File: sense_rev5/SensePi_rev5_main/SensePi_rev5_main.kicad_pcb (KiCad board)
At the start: 2 copper layers, 56.5 x 40 mm, 65 parts, among them J1 PJ-611-5A_AudioJack, J2 Conn_02x03_Odd_Even, Q1 IRLML6401, Q2 SI2302, SW1 SW_SPST, SW2 Slider_Switch_SW_2_State, U1 MDBT42Q, U2 MCP4012T-503E/CH, U3 TLV522, U4 PIR, U5 PCF8563T, Y1 Q13FC1350000400, Y2 Q13FC1350000400

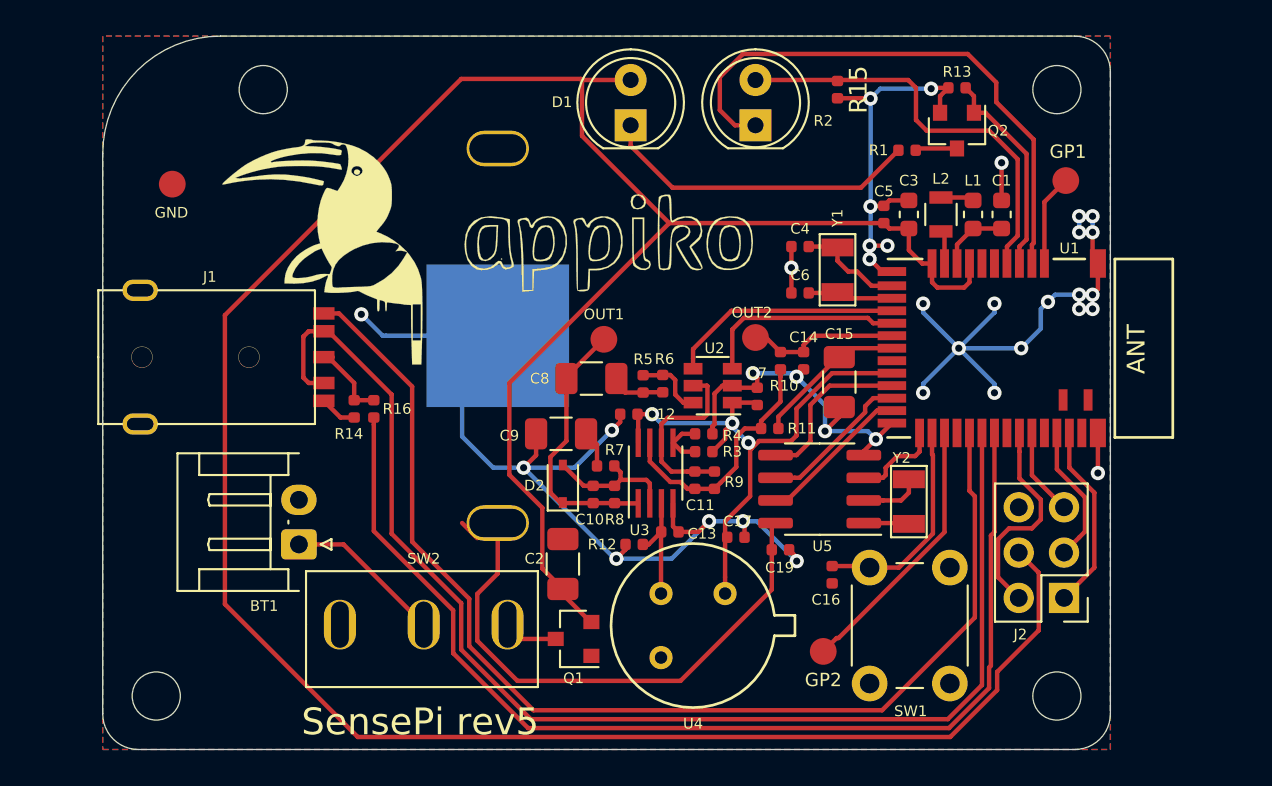
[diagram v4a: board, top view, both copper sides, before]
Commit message: Fix power switch GND conn and other minor fixes
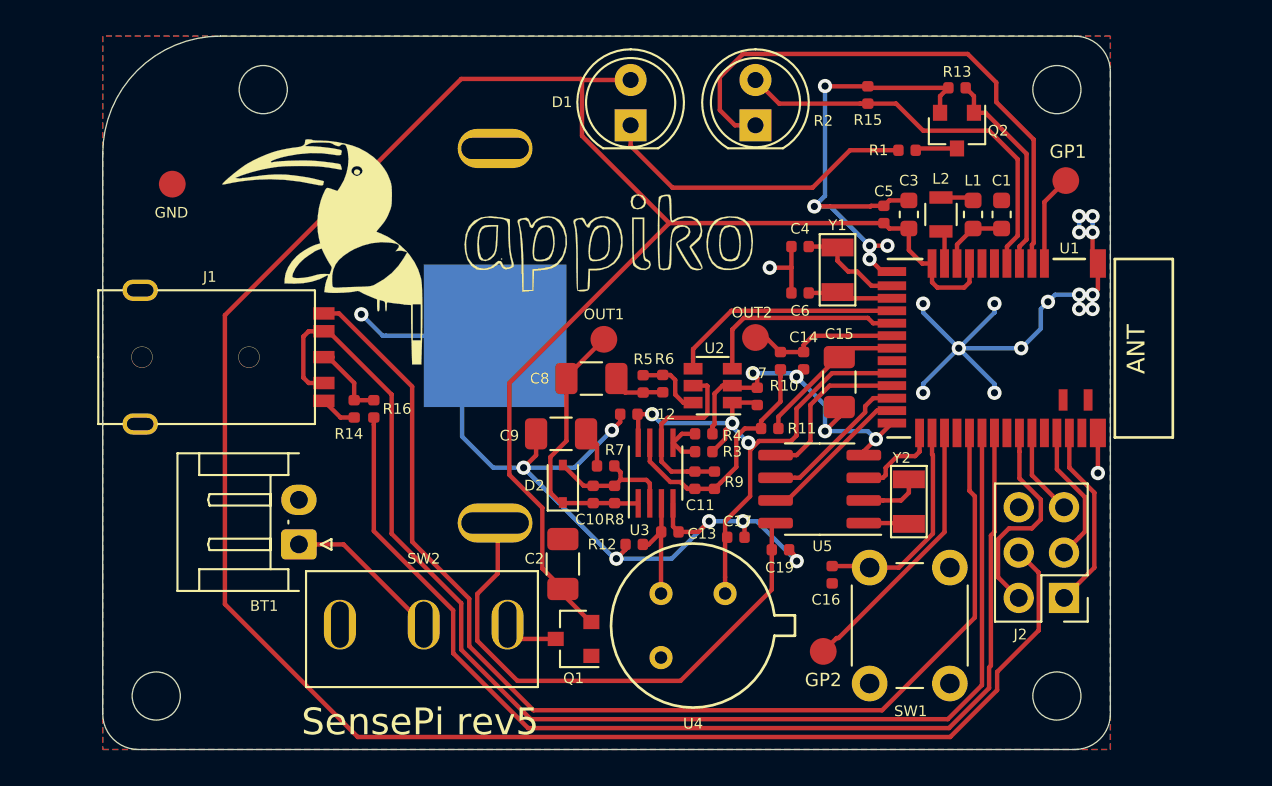
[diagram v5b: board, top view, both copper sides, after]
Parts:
- R14: value 1.2k -> NC
- R16: value 1k -> 470E
- moved G*** 5.02 mm to (56.1, 18.7)
- moved R15 1.73 mm to (52.9, 13.3), turned to 90 degrees
- moved BT2 0.15 mm to (32.0, 26.8)
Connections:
- SW2 pad 1: GND -> Net-(SW2-Pad1)
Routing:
- net GND: track 135.0 -> 140.7 mm, vias 35 -> 33
- net Net-(BT2-Pad1): track 31.7 -> 30.5 mm
- net /LDR_SENSE: track 23.7 -> 22.6 mm

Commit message: senseBe_rev4 and sense_rev5 gerber files updated.
senseBe_rev4 and sense_rev5 Slider switch footprint updated, sense_rev5 LDR resister position changed.
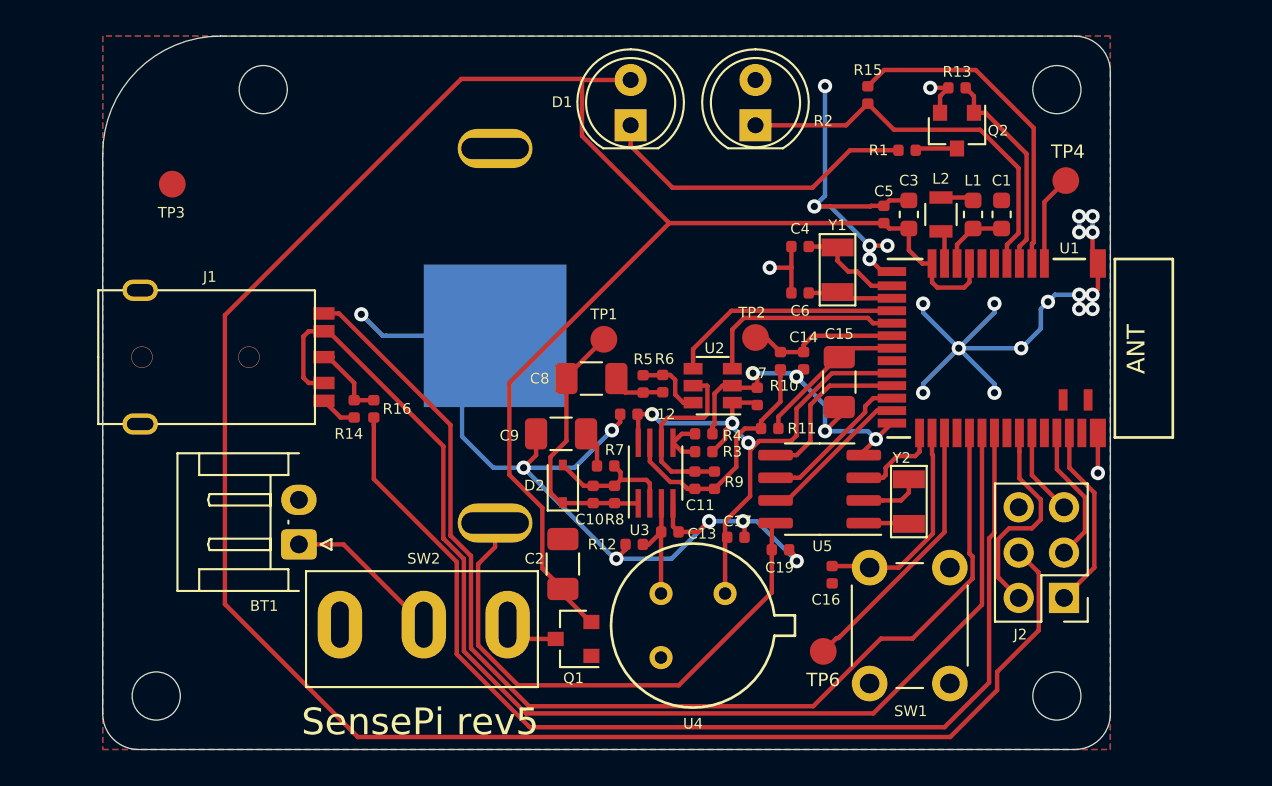
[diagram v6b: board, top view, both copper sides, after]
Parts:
- removed G***: LOGO, sense_fp:OSHW1
- removed G***: Appiko_Logo_2, sense_fp:Appiko_Logo_2
- removed G***: Appiko_LOGO_img, sense_fp:Appiko_LOGO_img
- TP6: renamed from GP2; value GP3 -> GP2
- turned R15 to 270 degrees
- renumbered OUT1 to TP1, OUT2 to TP2, GND to TP3, GP1 to TP4
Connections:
- R15 pad 1: /LDR_SENSE -> /LDR_SENSE_EN
- R15 pad 2: GND -> /LDR_SENSE
- R2 pad 1: /LDR_SENSE_EN -> /LDR_SENSE
- R2 pad 2: /LDR_SENSE -> GND
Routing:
- net /LDR_SENSE_EN: track 32.0 -> 18.7 mm
- net GND: track 140.7 -> 134.6 mm, vias 33 -> 34
- net /FOCUS: track 71.8 -> 68.8 mm
- net /TRIGGER: track 65.0 -> 63.4 mm

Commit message: Design sent for rev5_2 maufacturing
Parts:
- added G***: LOGO, sense_fp:OSHW1, B.Cu at (56.2, 18.8)
- added G***: Appiko_Logo_2, sense_fp:Appiko_Logo_2, F.Cu at (35.9, 20.9)
- added G***: Appiko_LOGO_img, sense_fp:Appiko_LOGO_img, F.Cu at (22.4, 21.7)
- renumbered TP3 to GND, TP4 to GP1, TP6 to GP2, TP1 to OUT1, TP2 to OUT2
